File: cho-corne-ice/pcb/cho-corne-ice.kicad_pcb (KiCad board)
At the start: 2 copper layers, 275.5 x 105.6 mm, 119 parts, among them J1 MJ-4PP-9, J2 OLED, J3 MJ-4PP-9, J4 OLED, SW1 SW_PUSH, SW10 SW_PUSH, SW11 SW_PUSH, SW12 SW_PUSH, SW13 SW_PUSH, SW14 SW_PUSH, SW15 SW_PUSH, SW16 SW_PUSH, SW17 SW_PUSH, SW18 SW_PUSH, SW19 SW_PUSH, SW2 SW_PUSH, SW20 SW_PUSH, SW21 SW_PUSH, SW22 SW_PUSH, SW23 SW_PUSH, SW24 SW_PUSH, SW25 SW_PUSH, SW26 SW_PUSH, SW27 SW_PUSH, SW28 SW_PUSH, SW29 SW_PUSH, SW3 SW_PUSH, SW30 SW_PUSH, SW31 SW_PUSH, SW32 SW_PUSH, SW33 SW_PUSH, SW34 SW_PUSH, SW35 SW_PUSH, SW36 SW_PUSH, SW37 SW_PUSH, SW38 SW_PUSH, SW39 SW_PUSH, SW4 SW_PUSH, SW40 SW_PUSH, SW41 SW_PUSH, SW42 SW_PUSH, SW5 SW_PUSH, SW6 SW_PUSH, SW7 SW_PUSH, SW8 SW_PUSH, SW9 SW_PUSH, U1 ProMicro, U2 ProMicro

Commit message: mx -> choc hotswap sockets
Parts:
- SW1, SW10, SW11, SW12, SW13, SW14, SW15, SW16, SW17, SW18, SW19, SW2, SW20, SW22, SW23, SW24, SW25, SW26, SW27, SW28, SW29, SW3, SW30, SW31, SW32, SW33, SW34, SW35, SW36, SW37, SW38, SW39, SW4, SW40, SW41, SW5, SW6, SW7, SW8, SW9: footprint kbd:CherryMX_Hotswap -> kbd:ChocV1_V2_Hotswap
- SW21, SW42: footprint kbd:CherryMX_Hotswap_1.5u -> kbd:ChocV1_V2_Hotswap_1.5u
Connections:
- J1 pad A: Net-(J1-PadA) -> unconnected-(J1-PadA)
- J3 pad A: Net-(J3-PadA) -> unconnected-(J3-PadA)
- U1 pad 1: LED -> unconnected-(U1-Pad1)
- U1 pad 11: Net-(U1-Pad11) -> unconnected-(U1-Pad11)
- U1 pad 12: Net-(U1-Pad12) -> unconnected-(U1-Pad12)
- U1 pad 13: Net-(U1-Pad13) -> unconnected-(U1-Pad13)
- U1 pad 14: Net-(U1-Pad14) -> unconnected-(U1-Pad14)
- U1 pad 24: Net-(U1-Pad24) -> unconnected-(U1-Pad24)
- U2 pad 1: LED_r -> unconnected-(U2-Pad1)
- U2 pad 11: Net-(U2-Pad11) -> unconnected-(U2-Pad11)
- U2 pad 12: Net-(U2-Pad12) -> unconnected-(U2-Pad12)
- U2 pad 13: Net-(U2-Pad13) -> unconnected-(U2-Pad13)
- U2 pad 14: Net-(U2-Pad14) -> unconnected-(U2-Pad14)
- U2 pad 24: Net-(U2-Pad24) -> unconnected-(U2-Pad24)
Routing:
- net GNDA: track 191.0 -> 0.00 mm
- net col0_r: track 175.8 -> 0.00 mm, vias 5 -> 0
- net col0: track 170.3 -> 0.00 mm, vias 5 -> 0
- net col1_r: track 150.7 -> 0.00 mm, vias 5 -> 0
- net col1: track 149.4 -> 0.00 mm, vias 5 -> 0
- net VCC: track 184.0 -> 48.8 mm, vias 2 -> 0
- net VDD: track 174.7 -> 41.2 mm, vias 2 -> 0
- net col3_r: track 133.0 -> 0.00 mm, vias 7 -> 0
- net col3: track 130.1 -> 0.00 mm, vias 7 -> 0
- net col2_r: track 128.2 -> 0.00 mm, vias 5 -> 0
- net col2: track 125.8 -> 0.00 mm, vias 5 -> 0
- net col4_r: track 115.5 -> 0.00 mm, vias 7 -> 0
- net col4: track 110.4 -> 0.00 mm, vias 7 -> 0
- net col5: track 104.1 -> 0.00 mm, vias 7 -> 0
- net row3_r: track 95.3 -> 0.00 mm, vias 2 -> 0
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
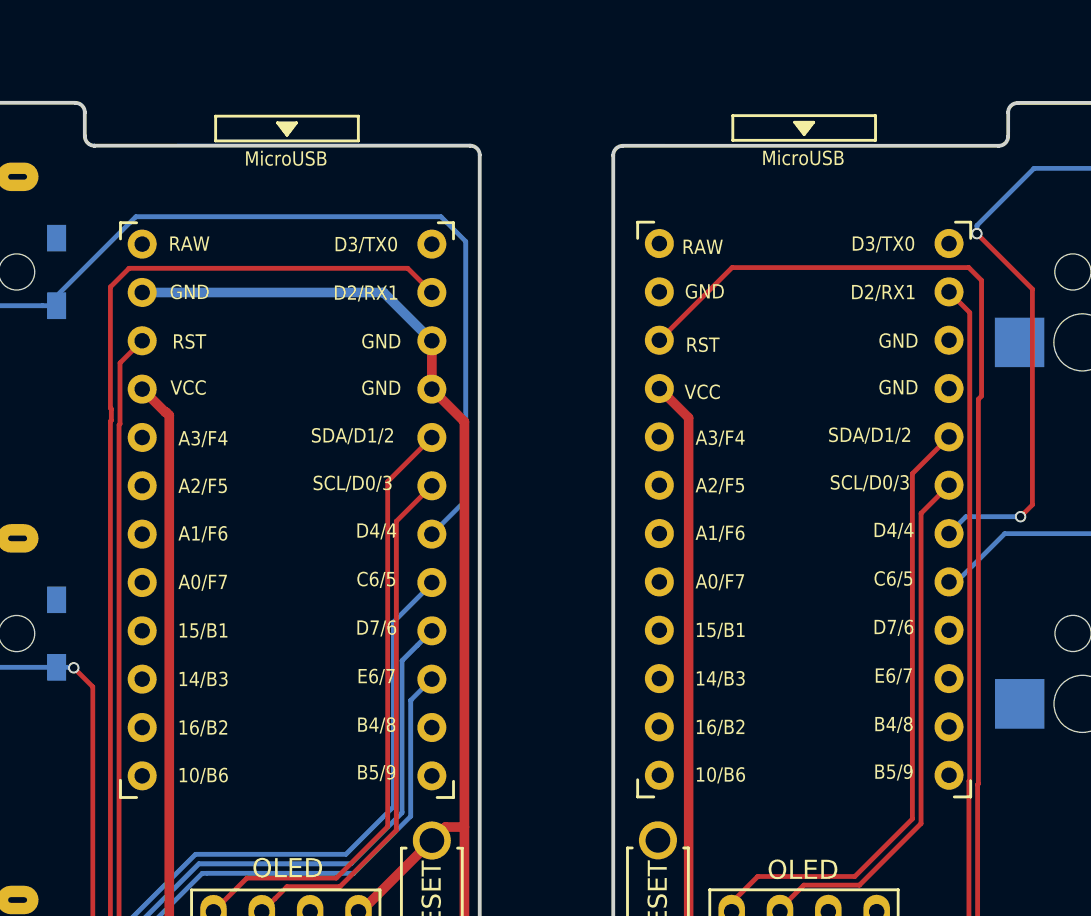
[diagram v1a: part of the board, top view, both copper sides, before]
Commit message: add nice!nano, replace Pro Micro footprints with nice!nano
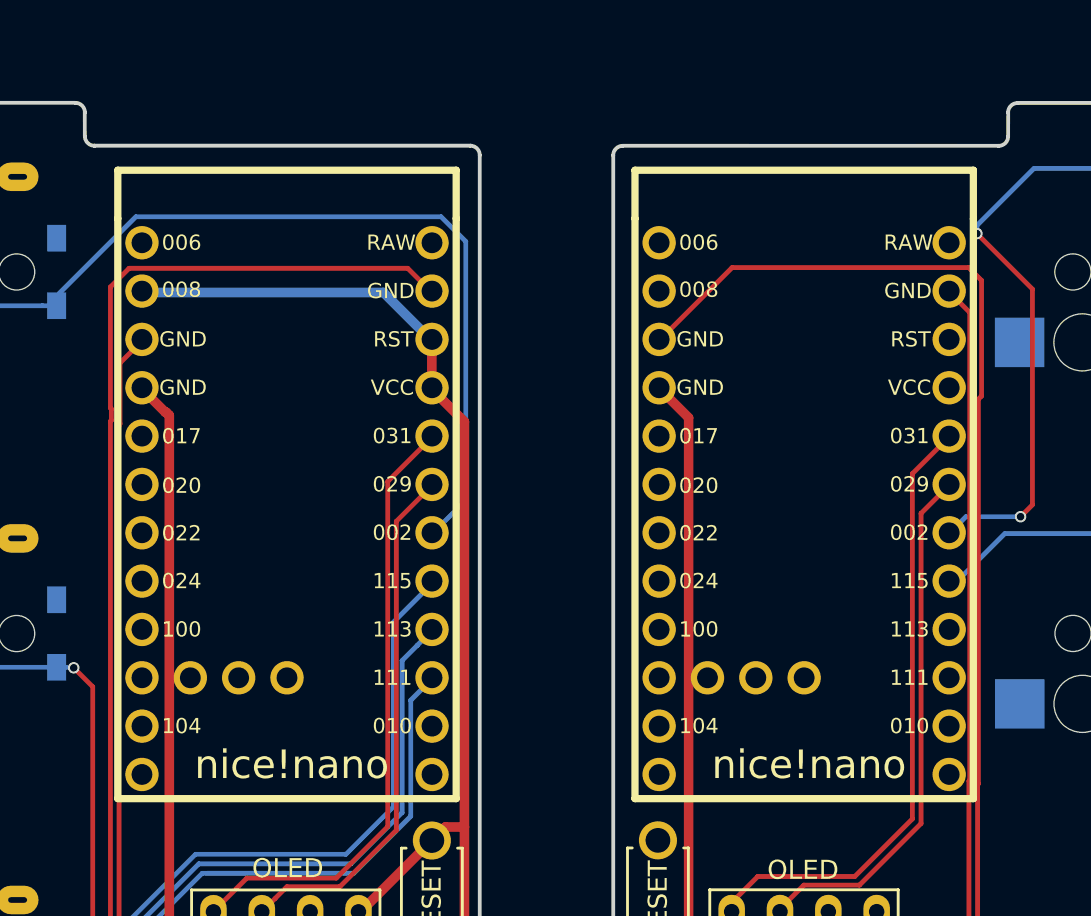
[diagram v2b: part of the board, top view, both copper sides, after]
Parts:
- U1, U2: value ProMicro -> nice_nano; footprint kbd:ProMicro_v3 -> nice-nano-kicad:nice_nano
- moved U1 0.58 mm to (134.8, 45.8), turned to -90 degrees
- moved U2 0.55 mm to (162.0, 45.8), turned to -90 degrees
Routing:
- net reset: track 60.0 -> 0.00 mm
- net GND: track 98.8 -> 158.8 mm
- net col0: track 0.00 -> 32.4 mm
- net SDA: track 32.4 -> 0.00 mm
- net col1: track 0.00 -> 27.7 mm
- net SCL: track 27.7 -> 0.00 mm

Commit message: wip
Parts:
- added J1: BAT, Connector_JST:JST_PH_S2B-PH-SM4-TB_1x02-1MP_P2.00mm_Horizontal, F.Cu at (126.8, -4.96)
- added PSW1: SW_SPDT, keeblib:switch_SSSS811101, F.Cu at (147.1, 63.6)
- renumbered J1 to J10
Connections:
- U1 pad 24: unconnected-(U1-Pad24) -> RAW
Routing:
- net data: track 77.0 -> 0.00 mm
- net GND: track 158.8 -> 235.8 mm
- net data_r: track 61.9 -> 0.00 mm
- net GNDA: track 0.00 -> 61.9 mm
- net col2_r: track 0.00 -> 44.2 mm, vias 0 -> 2
- net row0_r: track 124.6 -> 80.4 mm, vias 2 -> 0
- net col3_r: track 0.00 -> 24.4 mm
- net row1_r: track 103.7 -> 79.3 mm

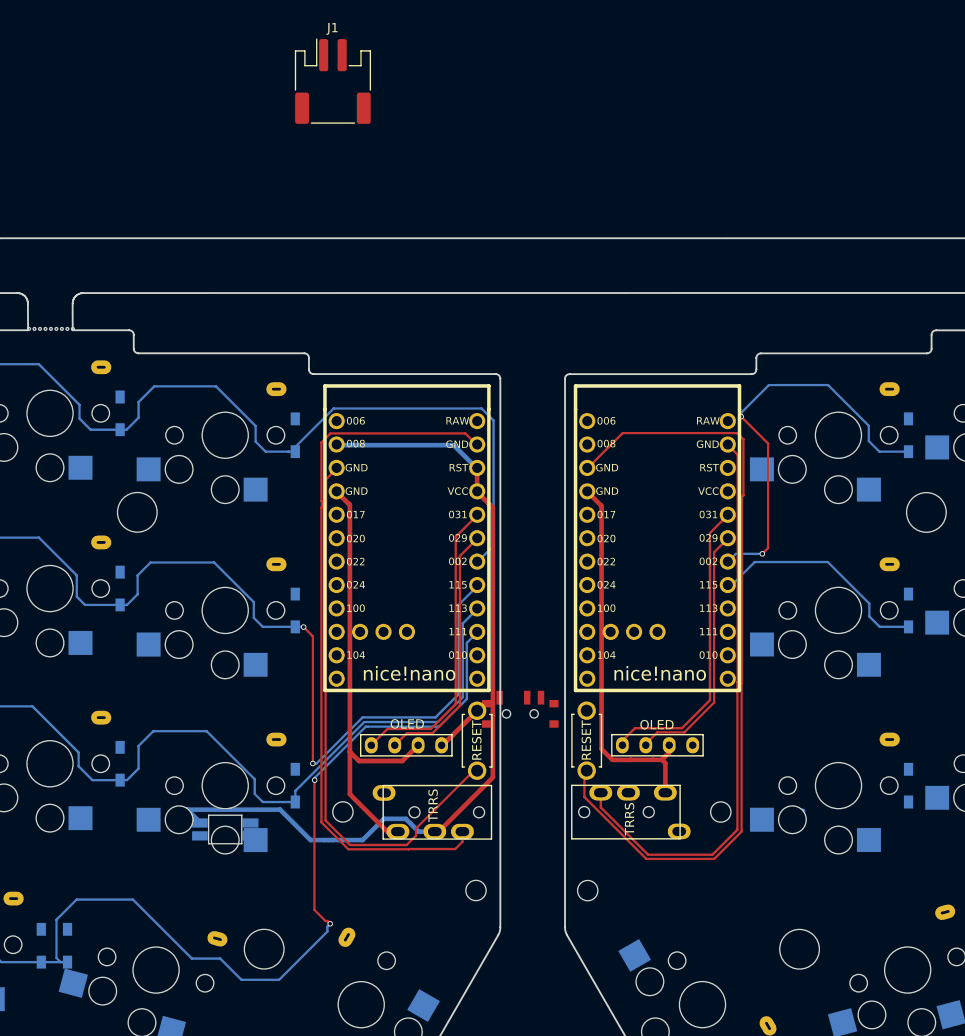
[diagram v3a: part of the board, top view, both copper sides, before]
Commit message: complete battery jumper and power switch, clean up nets again
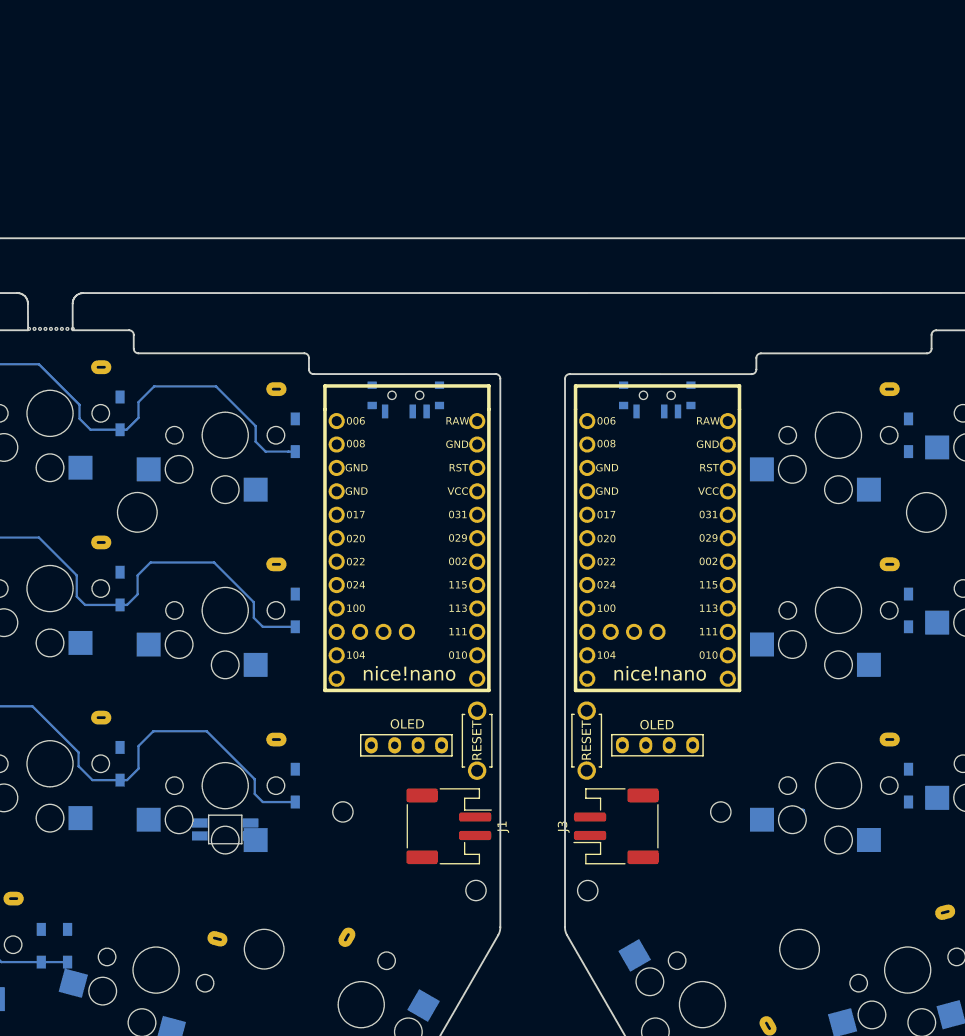
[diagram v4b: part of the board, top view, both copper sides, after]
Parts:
- removed J10: MJ-4PP-9, kbd:MJ-4PP-9_1side
- added PSW2: SW_SPDT, keeblib:switch_SSSS811101, B.Cu at (162.0, 29.1)
- J3: value MJ-4PP-9 -> BAT; footprint kbd:MJ-4PP-9_1side -> Connector_JST:JST_PH_S2B-PH-SM4-TB_1x02-1MP_P2.00mm_Horizontal
- PSW1: moved to B.Cu
- moved J1 81.7 mm to (139.4, 75.8), turned to -90 degrees
- moved PSW1 36.7 mm to (134.7, 29.1)
- moved J3 5.22 mm to (157.5, 75.8)
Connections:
- U2 pad 24: unconnected-(U2-Pad24) -> RAW_r
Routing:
- net GND: track 235.8 -> 0.11 mm
- net row3: track 121.7 -> 34.7 mm, vias 2 -> 0
- net reset_r: track 85.4 -> 0.00 mm
- net GNDA: track 61.9 -> 0.00 mm
- net VCC: track 48.8 -> 0.00 mm
- net row1: track 129.1 -> 81.4 mm, vias 2 -> 0
- net col2_r: track 44.2 -> 0.00 mm, vias 2 -> 0
- net VDD: track 41.2 -> 0.00 mm
- net row0: track 121.0 -> 80.6 mm
- net row2: track 115.7 -> 82.0 mm
- net SDA_r: track 32.7 -> 0.00 mm
- net col0: track 32.4 -> 0.00 mm
- net SCL_r: track 27.9 -> 0.00 mm
- net col1: track 27.7 -> 0.00 mm
- net col3_r: track 24.4 -> 0.00 mm

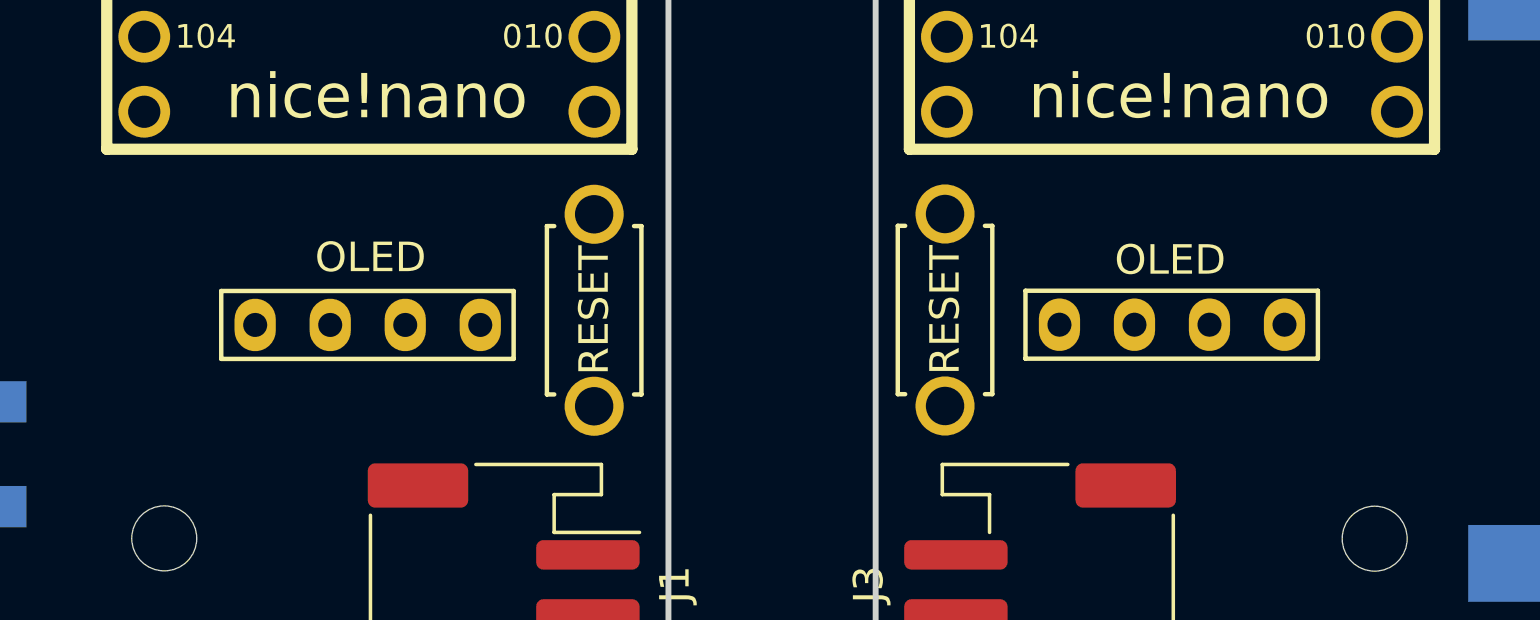
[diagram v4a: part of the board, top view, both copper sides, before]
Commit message: finish switches and nice!view
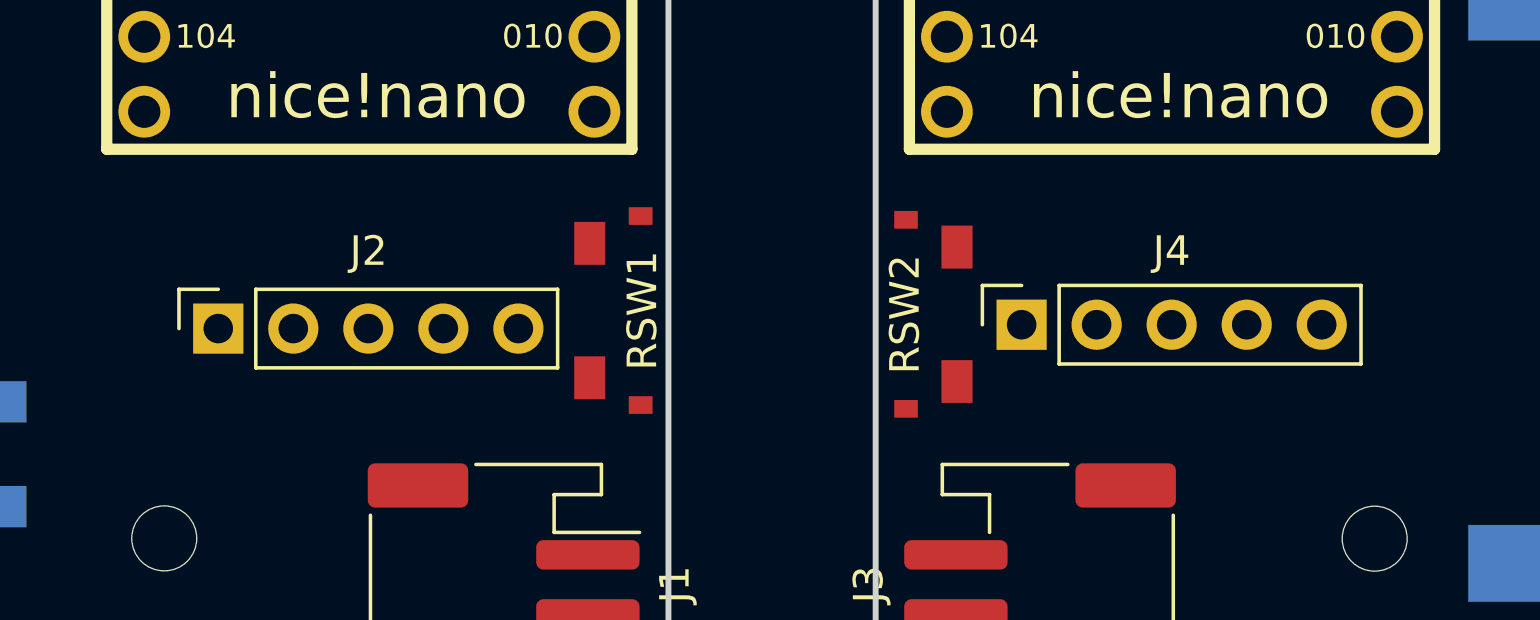
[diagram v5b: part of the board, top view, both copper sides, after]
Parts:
- J2, J4: value OLED -> nice!view; footprint kbd:OLED_1side -> Connector_PinSocket_2.54mm:PinSocket_1x05_P2.54mm_Vertical
- RSW1, RSW2: footprint kbd:ResetSW_1side -> keeblib:alps_sksn
- moved RSW1 2.43 mm to (144.8, 66.5), turned to 90 degrees
- moved RSW2 2.18 mm to (152.1, 66.7)
- moved J4 1.28 mm to (156.9, 67.0), turned to 90 degrees
- moved J2 1.26 mm to (129.7, 67.2), turned to 90 degrees
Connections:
- net SCL renamed SCK
- net SCL_r renamed SCK_r
- net SDA renamed MOSI
- net SDA_r renamed MOSI_r
- U1 pad 1: unconnected-(U1-Pad1) -> CS
- U1 pad 2: data -> unconnected-(U1-Pad2)
- U2 pad 1: unconnected-(U2-Pad1) -> CS_r
- U2 pad 2: data_r -> unconnected-(U2-Pad2)

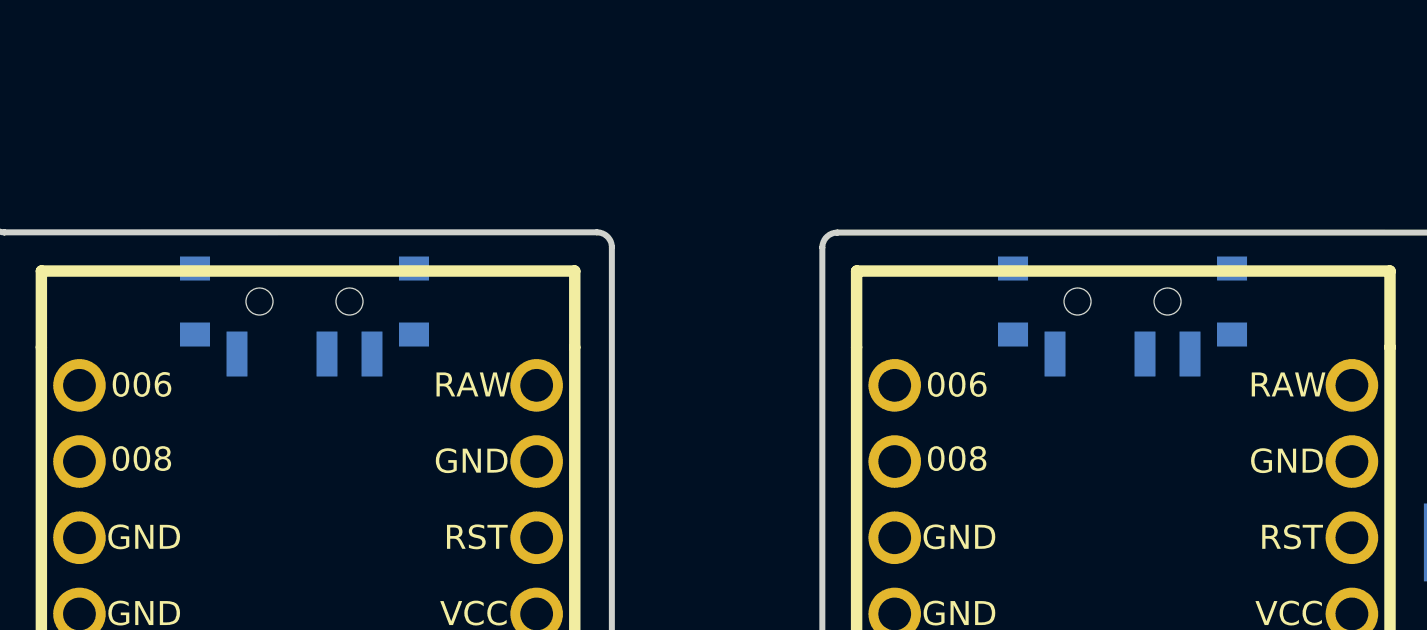
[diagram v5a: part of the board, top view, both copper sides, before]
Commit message: tweak footprints
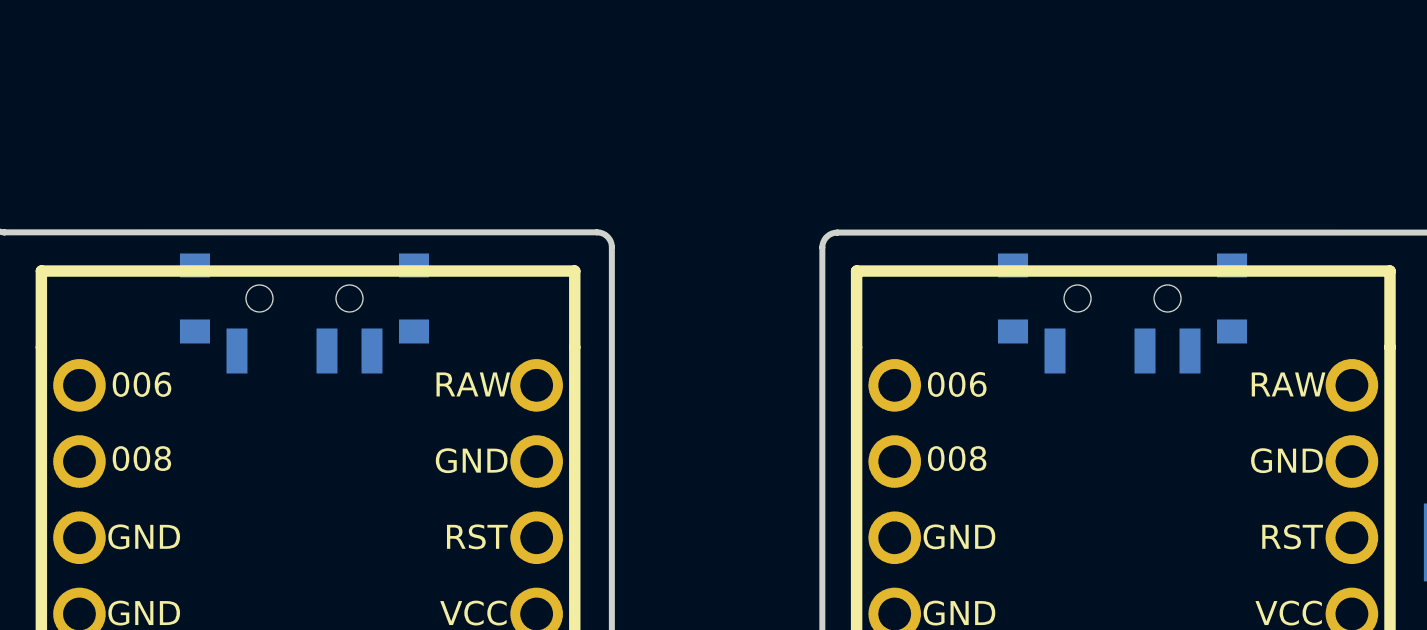
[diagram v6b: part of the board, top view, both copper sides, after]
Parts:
- moved PSW1 0.10 mm to (134.7, 29.0)
- moved PSW2 0.10 mm to (162.0, 29.0)
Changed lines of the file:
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@@
   )
   (footprint "keeblib:switch_SSSS811101" (layer "B.Cu")
-    (at 161.9625 29.076)
+    (at 161.9625 28.9744)
     (property "Sheetfile" "File: cho-corne-ice.kicad_sch")
     (property "Sheetname" "")
@@
   )
   (footprint "keeblib:switch_SSSS811101" (layer "B.Cu")
-    (at 134.693787 29.076)
+    (at 134.693787 28.9744)
     (property "Sheetfile" "File: cho-corne-ice.kicad_sch")
     (property "Sheetname" "")
